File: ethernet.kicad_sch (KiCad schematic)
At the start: 66 parts, among them Q6001 DMG1012T, Q6002 DMG1012T, U1001 AM6231ASGGGAALW, U6001 HR911130A, U6002 RTL8211F-CG, X6001 ECS-2520MV-250-BN-TR

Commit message: Restarted SoC power decoupling based on manufacturer capabilities
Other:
- note added: "Gigabit Ethernet"
- moved on the sheet: C6001, C6002, C6003, C6004, C6005, C6006, C6007, C6008, C6009, C6010, C6011, C6012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

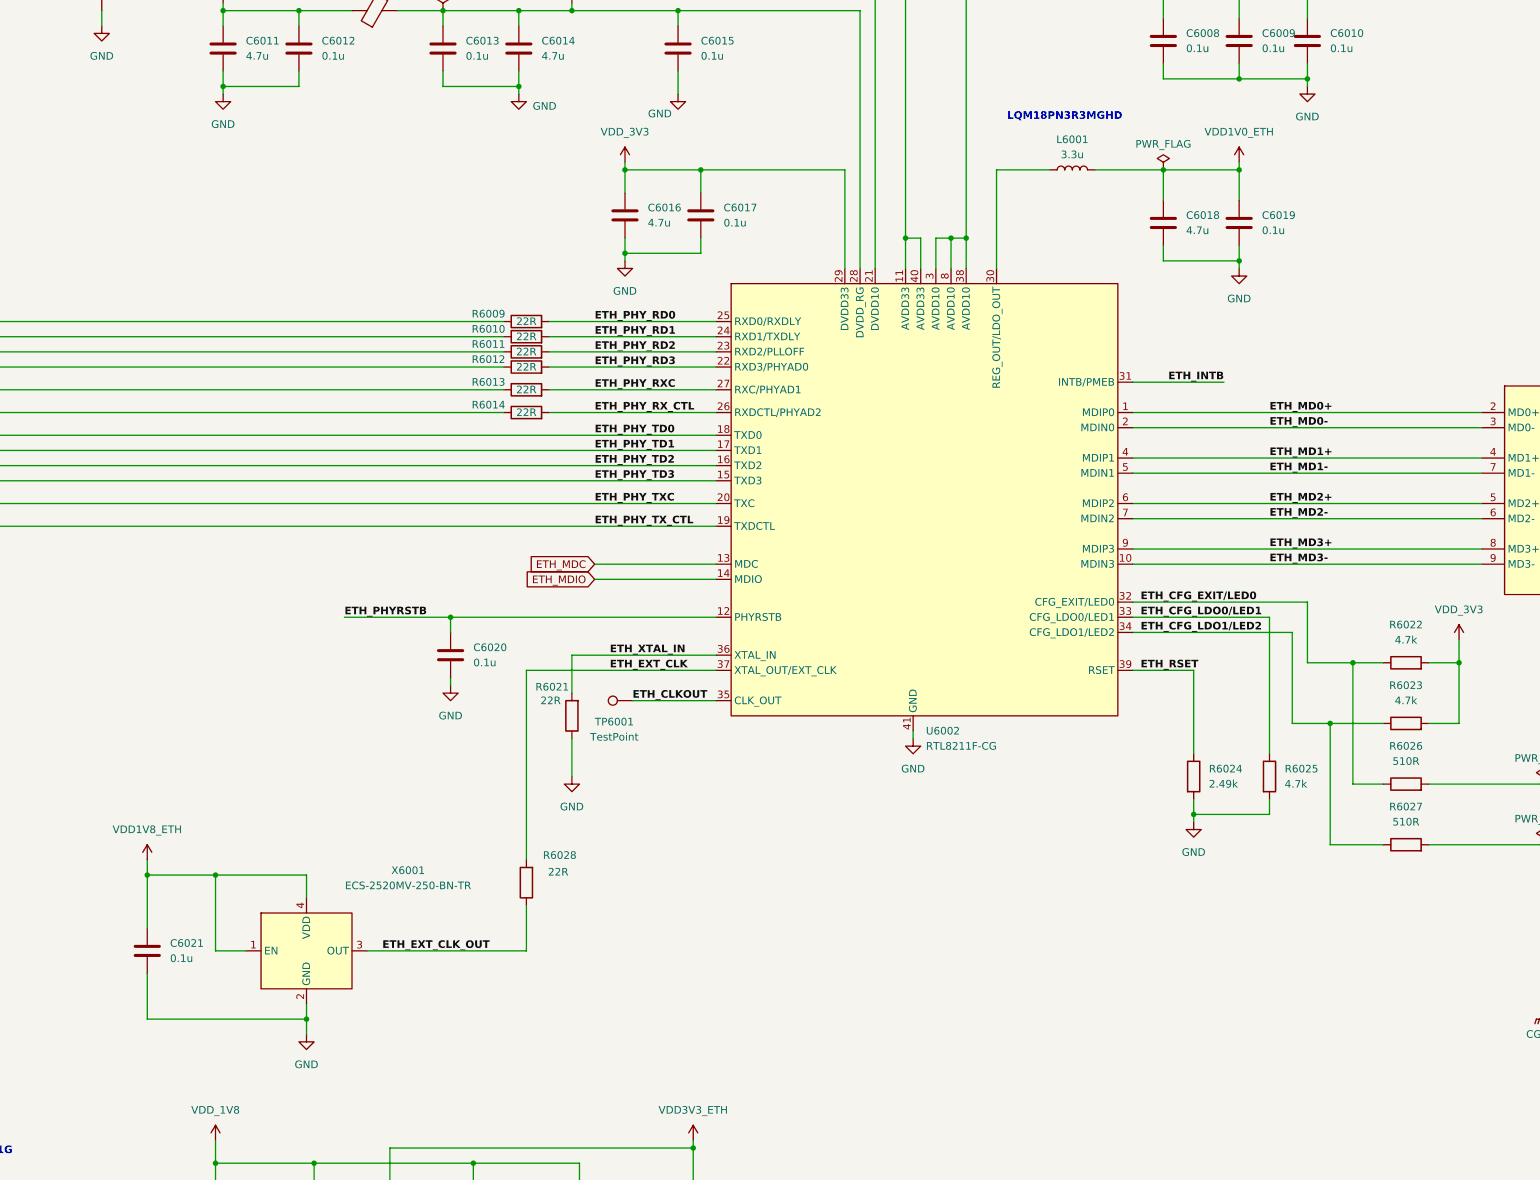
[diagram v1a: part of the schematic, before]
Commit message: Started USB and OSC routing
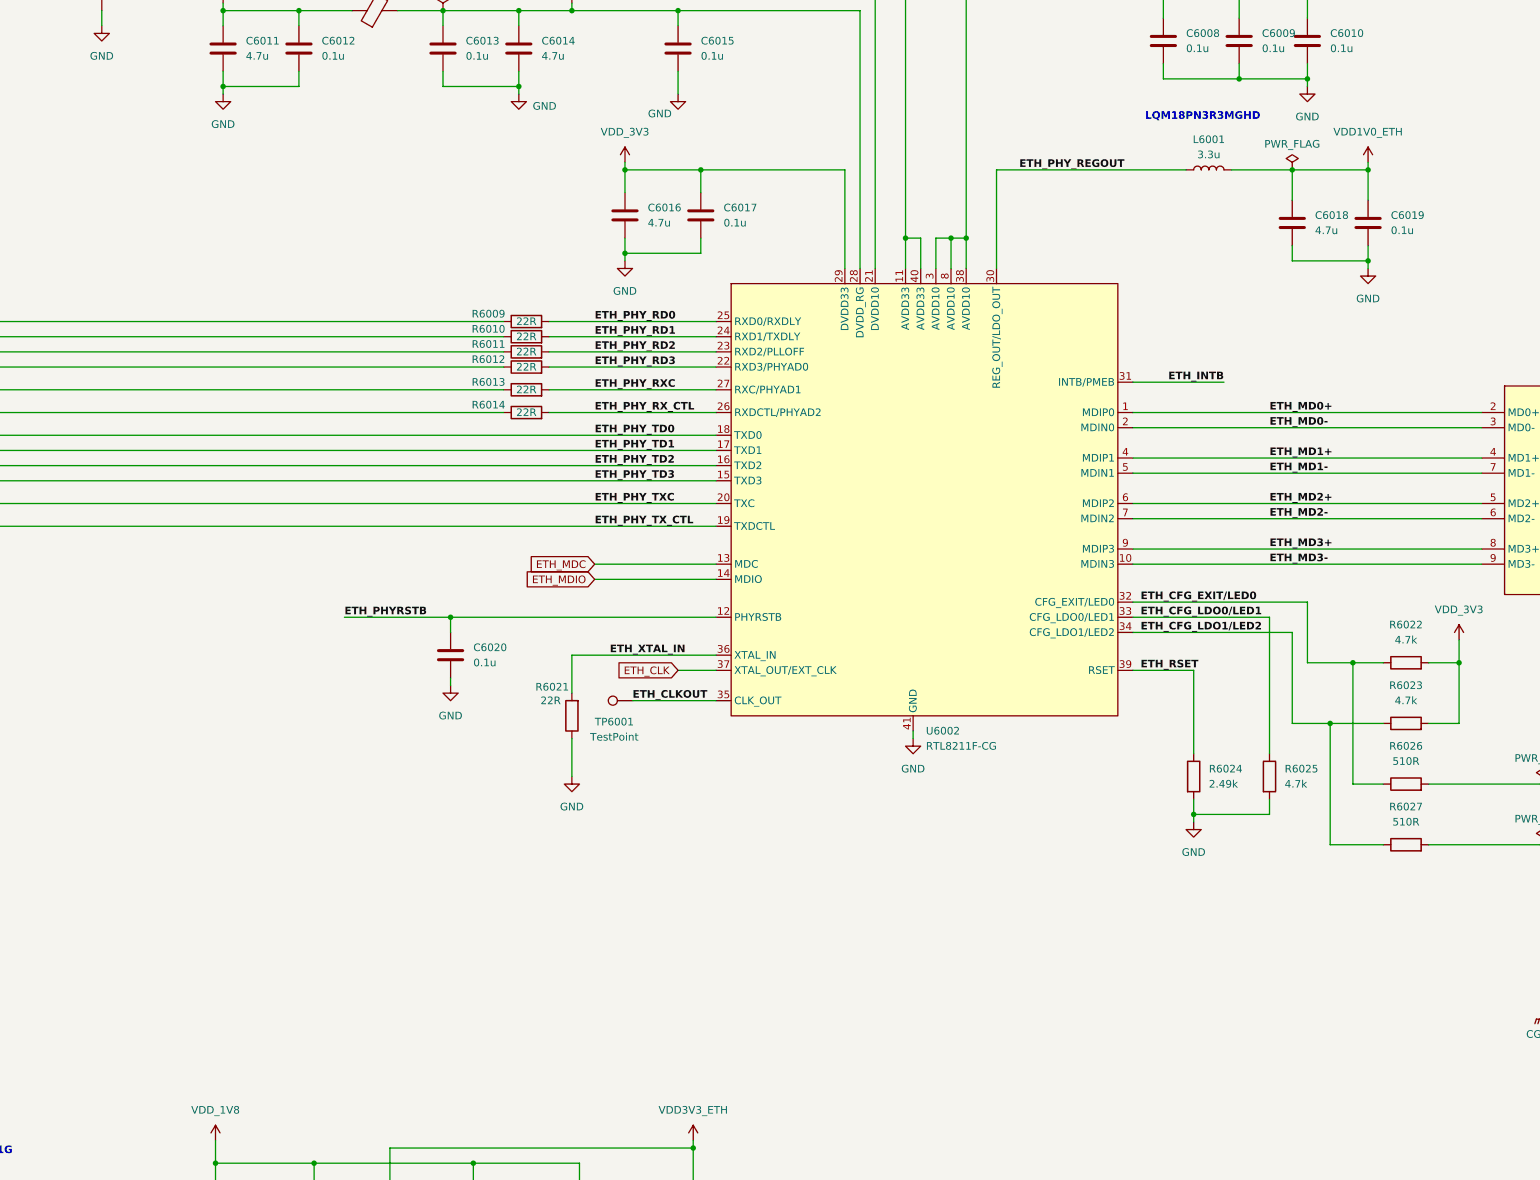
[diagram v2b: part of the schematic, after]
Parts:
- removed C6021: 0.1u, symbol Device:C
- removed R6028: 22R, symbol Device:R
- removed X6001: ECS-2520MV-250-BN-TR, ECS-2520MV-250-BN-TR:ECS2520MV250BNTR, symbol SoftServicesSymbolLibrary:ECS-2520MV-250-BN-TR
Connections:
- net ETH_PHY_REGOUT: now reaches L6001.1, U6002.30 (REG_OUT/LDO_OUT)
- net ETH_EXT_CLK renamed ETH_CLK
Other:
- moved on the sheet: C6018, C6019, L6001

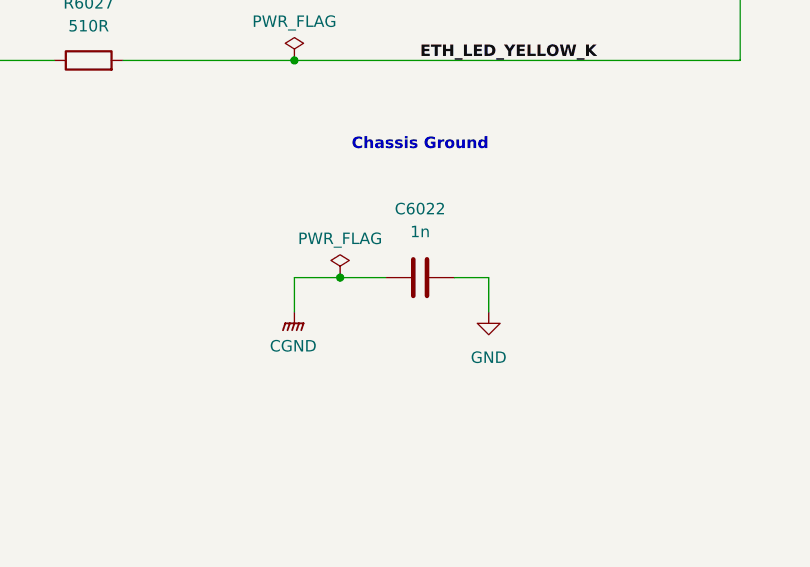
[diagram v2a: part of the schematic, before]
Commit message: Continued Ethernet routing
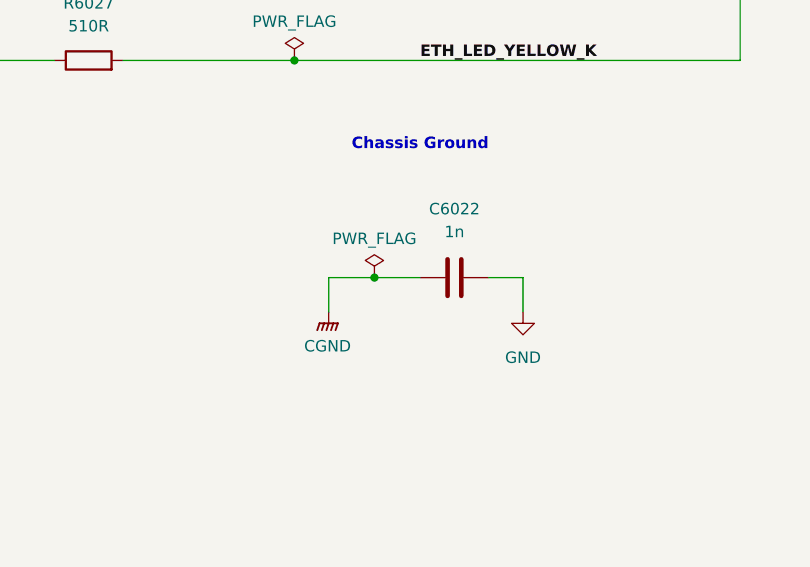
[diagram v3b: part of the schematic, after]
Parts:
- C6001, C6002, C6004, C6005, C6007, C6008, C6009, C6010, C6012, C6013, C6015, C6017, C6019, C6020: footprint (none) -> Capacitor_SMD:C_0201_0603Metric
- C6003, C6006, C6011, C6014, C6016, C6018: footprint (none) -> Capacitor_SMD:C_0402_1005Metric
- C6022: footprint (none) -> Capacitor_SMD:C_1206_3216Metric
- R6001, R6002, R6003, R6005, R6006, R6007, R6008, R6009, R6010, R6011, R6012, R6013, R6014, R6015, R6016, R6017, R6018, R6019, R6020, R6021: footprint (none) -> Resistor_SMD:R_0201_0603Metric
- R6022, R6023, R6024, R6025, R6026, R6027, R6029, R6030, R6031, R6032: footprint (none) -> Resistor_SMD:R_0402_1005Metric
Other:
- moved on the sheet: C6022

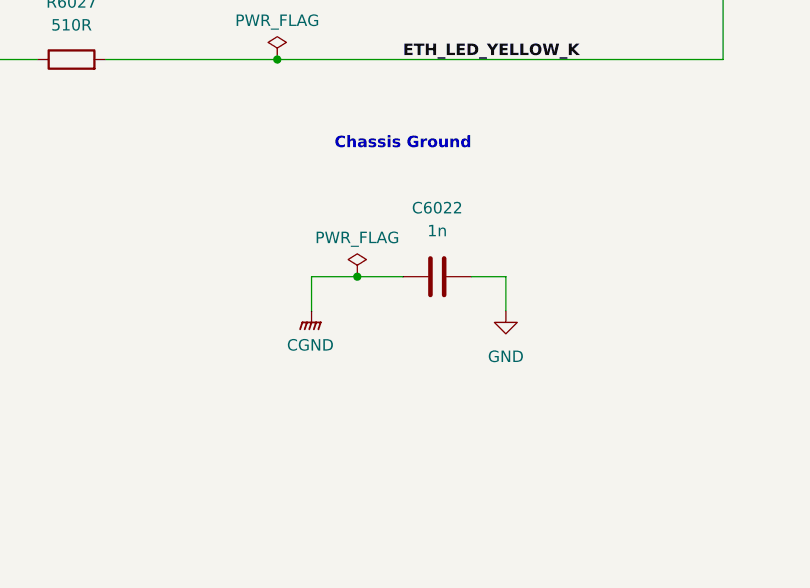
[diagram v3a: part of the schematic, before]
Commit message: Added RJ45 connector chassis ground plane and vias
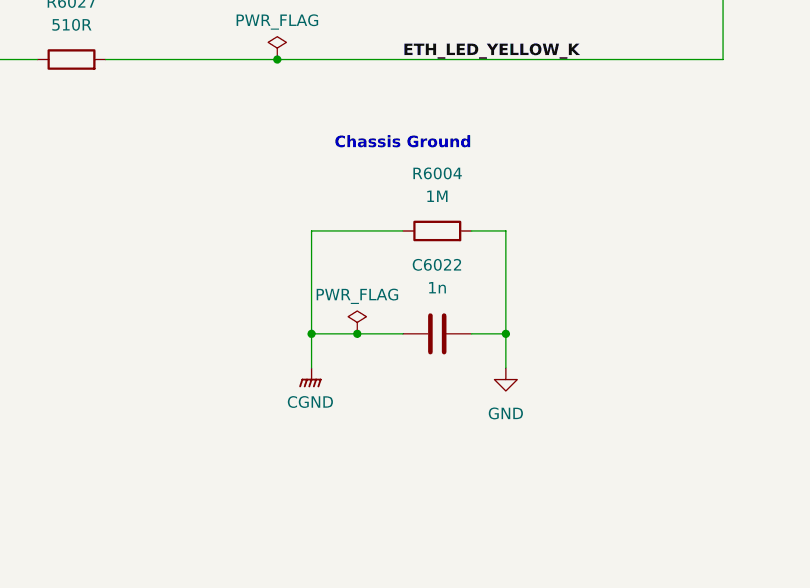
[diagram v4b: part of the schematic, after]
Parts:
- added R6004: 1M, Resistor_SMD:R_1206_3216Metric, symbol Device:R
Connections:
- net CGND: now also R6004.1
- net GND: now also R6004.2
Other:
- moved on the sheet: C6022
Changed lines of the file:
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@@
 	)
 	(junction
-		(at 419.1 294.64)
+		(at 419.1 300.99)
 		(diameter 0)
 		(color 0 0 0 0)
@@
 	)
 	(junction
+		(at 414.02 300.99)
+		(diameter 0)
+		(color 0 0 0 0)
+	)
+	(junction
 		(at 168.91 119.38)
 		(diameter 0)
@@
 	)
 	(junction
+		(at 435.61 300.99)
+		(diameter 0)
+		(color 0 0 0 0)
+	)
+	(junction
 		(at 516.89 101.6)
 		(diameter 0)
@@
 	(wire
 		(pts
-			(xy 414.02 298.45) (xy 414.02 294.64)
+			(xy 414.02 304.8) (xy 414.02 300.99)
 		)
 		(stroke
@@
 	(wire
 		(pts
+			(xy 414.02 289.56) (xy 414.02 300.99)
+		)
+		(stroke
+			(width 0)
+			(type default)
+		)
+	)
+	(wire
+		(pts
 			(xy 257.81 246.38) (xy 271.78 246.38)
 		)
@@
 	(wire
 		(pts
-			(xy 419.1 294.64) (xy 424.18 294.64)
+			(xy 419.1 300.99) (xy 424.18 300.99)
 		)
 		(stroke
@@
 	(wire
 		(pts
-			(xy 431.8 294.64) (xy 435.61 294.64)
+			(xy 431.8 300.99) (xy 435.61 300.99)
 		)
 		(stroke
@@
 	(wire
 		(pts
+			(xy 431.8 289.56) (xy 435.61 289.56)
+		)
+		(stroke
+			(width 0)
+			(type default)
+		)
+	)
+	(wire
+		(pts
 			(xy 370.84 128.27) (xy 370.84 132.08)
 		)
@@
 	(wire
 		(pts
+			(xy 435.61 289.56) (xy 435.61 300.99)
+		)
+		(stroke
+			(width 0)
+			(type default)
+		)
+	)
+	(wire
+		(pts
 			(xy 313.69 128.27) (xy 313.69 168.91)
 		)
@@
 	(wire
 		(pts
+			(xy 424.18 289.56) (xy 414.02 289.56)
+		)
+		(stroke
+			(width 0)
+			(type default)
+		)
+	)
+	(wire
+		(pts
 			(xy 359.41 139.7) (xy 359.41 142.24)
 		)
@@
 	(wire
 		(pts
-			(xy 435.61 294.64) (xy 435.61 298.45)
+			(xy 435.61 300.99) (xy 435.61 304.8)
 		)
 		(stroke
@@
 	(wire
 		(pts
-			(xy 414.02 294.64) (xy 419.1 294.64)
+			(xy 414.02 300.99) (xy 419.1 300.99)
 		)
 		(stroke
@@
 	(symbol
 		(lib_id "Device:C")
-		(at 427.99 294.64 90)
+		(at 427.99 300.99 90)
 		(unit 1)
 		(exclude_from_sim no)
@@
 		(fields_autoplaced yes)
 		(property "Reference" "C6022"
-			(at 427.99 287.02 90)
+			(at 427.99 293.37 90)
 			(effects
 				(font
@@
 		)
 		(property "Value" "1n"
-			(at 427.99 289.56 90)
+			(at 427.99 295.91 90)
 			(effects
 				(font
@@
 		)
 		(property "Footprint" "Capacitor_SMD:C_1206_3216Metric"
-			(at 431.8 293.6748 0)
+			(at 431.8 300.0248 0)
 			(effects
 				(font
@@
 		)
 		(property "Datasheet" "~"
-			(at 427.99 294.64 0)
+			(at 427.99 300.99 0)
 			(effects
 				(font
@@
 		)
 		(property "Description" "Unpolarized capacitor"
-			(at 427.99 294.64 0)
+			(at 427.99 300.99 0)
 			(effects
 				(font
@@
 	(symbol
 		(lib_id "Device:R")
+		(at 427.99 289.56 90)
+		(unit 1)
+		(exclude_from_sim no)
+		(in_bom yes)
+		(on_board yes)
+		(dnp no)
+		(fields_autoplaced yes)
+		(property "Reference" "R6004"
+			(at 427.99 283.21 90)
+			(effects
+				(font
+					(size 1.27 1.27)
+				)
+			)
+		)
+		(property "Value" "1M"
+			(at 427.99 285.75 90)
+			(effects
+				(font
+					(size 1.27 1.27)
+				)
+			)
+		)
+		(property "Footprint" "Resistor_SMD:R_1206_3216Metric"
+			(at 427.99 291.338 90)
+			(effects
+				(font
+					(size 1.27 1.27)
+				)
+				(hide yes)
+			)
+		)
+		(property "Datasheet" "~"
+			(at 427.99 289.56 0)
+			(effects
+				(font
+					(size 1.27 1.27)
+				)
+				(hide yes)
+			)
+		)
+		(property "Description" "Resistor"
+			(at 427.99 289.56 0)
+			(effects
+				(font
+					(size 1.27 1.27)
+				)
+				(hide yes)
+			)
+		)
+		(pin "2"
+		)
+		(pin "1"
+		)
+		(instances
+			(project ""
+				(path "/b43b7bca-e50d-42ec-8ff0-e0016dfefe0a/6c7f2037-3077-4980-ab71-7ff032fdfd6e"
+					(reference "R6004")
+					(unit 1)
+				)
+			)
+		)
+	)
+	(symbol
+		(lib_id "Device:R")
 		(at 387.35 250.19 90)
 		(unit 1)
@@
 	(symbol
 		(lib_id "power:PWR_FLAG")
-		(at 419.1 294.64 0)
+		(at 419.1 300.99 0)
 		(unit 1)
 		(exclude_from_sim no)
@@
 		(dnp no)
 		(property "Reference" "#FLG04033"
-			(at 419.1 292.735 0)
+			(at 419.1 299.085 0)
 			(effects
 				(font
@@
 		)
 		(property "Value" "PWR_FLAG"
-			(at 419.1 290.322 0)
+			(at 419.1 296.672 0)
 			(effects
 				(font
@@
 		)
 		(property "Footprint" ""
-			(at 419.1 294.64 0)
+			(at 419.1 300.99 0)
 			(effects
 				(font
@@
 		)
 		(property "Datasheet" "~"
-			(at 419.1 294.64 0)
+			(at 419.1 300.99 0)
 			(effects
 				(font
@@
 		)
 		(property "Description" "Special symbol for telling ERC where power comes from"
-			(at 419.1 294.64 0)
+			(at 419.1 300.99 0)
 			(effects
 				(font
@@
 	(symbol
 		(lib_id "power:GNDPWR")
-		(at 414.02 298.45 0)
+		(at 414.02 304.8 0)
 		(unit 1)
 		(exclude_from_sim no)
@@
 		(fields_autoplaced yes)
 		(property "Reference" "#PWR06031"
-			(at 414.02 303.53 0)
+			(at 414.02 309.88 0)
 			(effects
 				(font
@@
 		)
 		(property "Value" "CGND"
-			(at 413.893 302.26 0)
+			(at 413.893 308.61 0)
 			(effects
 				(font
@@
 		)
 		(property "Footprint" ""
-			(at 414.02 299.72 0)
+			(at 414.02 306.07 0)
 			(effects
 				(font
@@
 		)
 		(property "Datasheet" ""
-			(at 414.02 299.72 0)
+			(at 414.02 306.07 0)
 			(effects
 				(font
@@
 		)
 		(property "Description" "Power symbol creates a global label with name \"GNDPWR\" , global ground"
-			(at 414.02 298.45 0)
+			(at 414.02 304.8 0)
 			(effects
 				(font
@@
 	(symbol
 		(lib_id "power:GND")
-		(at 435.61 298.45 0)
+		(at 435.61 304.8 0)
 		(unit 1)
 		(exclude_from_sim no)
@@
 		(fields_autoplaced yes)
 		(property "Reference" "#PWR06032"
-			(at 435.61 304.8 0)
+			(at 435.61 311.15 0)
 			(effects
 				(font
@@
 		)
 		(property "Value" "GND"
-			(at 435.61 303.53 0)
+			(at 435.61 309.88 0)
 			(effects
 				(font
@@
 		)
 		(property "Footprint" ""
-			(at 435.61 298.45 0)
+			(at 435.61 304.8 0)
 			(effects
 				(font
@@
 		)
 		(property "Datasheet" ""
-			(at 435.61 298.45 0)
+			(at 435.61 304.8 0)
 			(effects
 				(font
@@
 		)
 		(property "Description" "Power symbol creates a global label with name \"GND\" , ground"
-			(at 435.61 298.45 0)
+			(at 435.61 304.8 0)
 			(effects
 				(font
